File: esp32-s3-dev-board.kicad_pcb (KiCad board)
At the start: 2 copper layers, 30.8 x 50 mm, 16 parts, among them IC1 ESP32-S3-WROOM-1-N8R8, J1 Conn_01x18, J2 Conn_01x18, J3 PROG_HDR, Q1 SS8050-G, Q2 SS8050-G

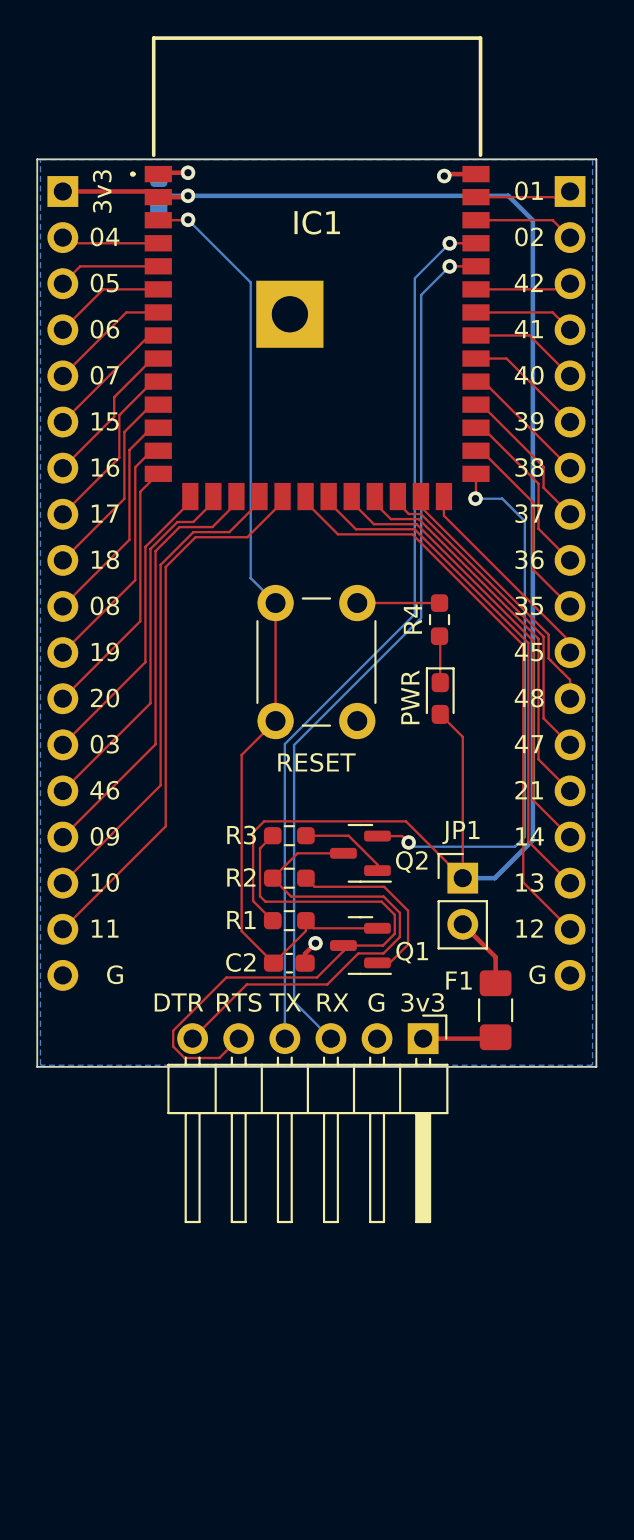
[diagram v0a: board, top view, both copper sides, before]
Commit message: Updated template for KiCAD 7
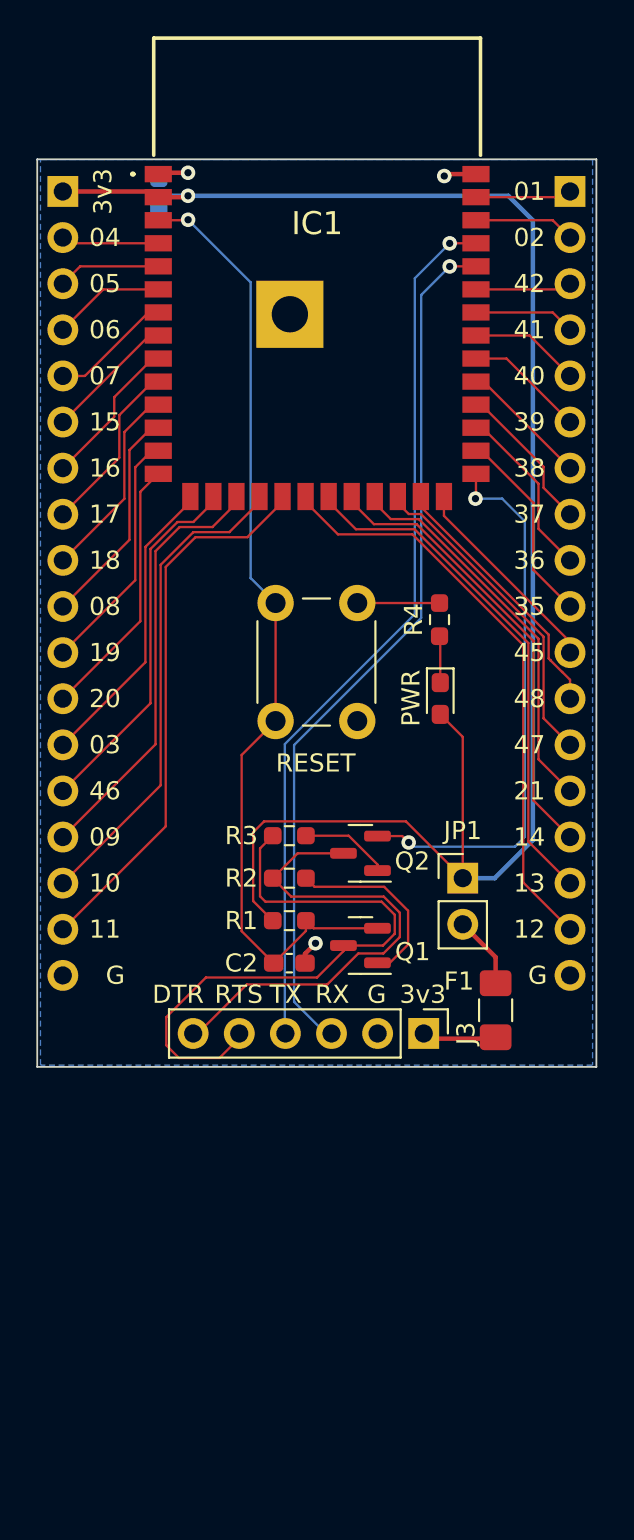
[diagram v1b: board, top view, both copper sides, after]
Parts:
- IC1: footprint footprints:ESP32S3WROOM1N8R8 -> Chof747 Footprints:ESP32S3WROOM1N8R8
- J3: footprint Connector_PinHeader_2.54mm:PinHeader_1x06_P2.54mm_Horizontal -> Connector_PinHeader_2.54mm:PinHeader_1x06_P2.54mm_Vertical
- moved J3 0.29 mm to (69.9, 119.8)
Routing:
- net RTS: track 32.3 -> 33.5 mm

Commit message: Changed reset circuit to UMH3N and Upgrade to KiCad 8
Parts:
- removed PWR: PWR, LED_SMD:LED_0603_1608Metric_Pad1.05x0.95mm_HandSolder
- removed Q2: SS8050-G, Package_TO_SOT_SMD:SOT-23
- removed R3: 10k, Resistor_SMD:R_0603_1608Metric_Pad0.98x0.95mm_HandSolder
- removed R4: 1k, Resistor_SMD:R_0603_1608Metric_Pad0.98x0.95mm_HandSolder
- removed RESET: SW_Reset, Button_Switch_THT:SW_PUSH_6mm
- added D1: PWR, LED_SMD:LED_0603_1608Metric_Pad1.05x0.95mm_HandSolder, F.Cu at (72.1, 106.1)
- added G***: LOGO, Chof747 Logos:LOGO large, B.Cu at (55.9, 87.6)
- added SW1: SW_Reset, Button_Switch_THT:SW_PUSH_6mm, F.Cu at (66.2, 96.0)
- Q1: value SS8050-G -> UMH3N; footprint Package_TO_SOT_SMD:SOT-23 -> Package_TO_SOT_SMD:SOT-363_SC-70-6
- R2: value 10k -> 1k
- moved R2 13.5 mm to (72.1, 101.8), turned to 90 degrees
- moved C2 2.21 mm to (61.6, 113.9), turned to 90 degrees
- moved R1 1.07 mm to (63.5, 113.9), turned to -90 degrees
- moved Q1 1.02 mm to (66.4, 113.9), turned to 90 degrees
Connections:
- Q1 pad 1: Net-(Q1-Pad1) -> RTS
- Q1 pad 2: ~{RESET} -> DTR
- Q1 pad 3: RTS ->  GPIO0
- R2 pad 1: DTR -> Net-(D1-K)
- R2 pad 2: Net-(Q1-Pad1) -> GND
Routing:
- net +3V3: track 95.3 -> 81.3 mm
- net DTR: track 27.3 -> 14.0 mm
- net RTS: track 33.5 -> 22.9 mm
- net Net-(Q1-Pad1): track 10.3 -> 0.00 mm
- net GND: track 9.33 -> 14.9 mm
- net Net-(Q2-Pad1): track 4.93 -> 0.00 mm
- net  GPIO0: track 30.6 -> 34.0 mm
- net Net-(D1-Pad1): track 2.57 -> 0.00 mm
- net Net-(D1-K): track 0.00 -> 2.51 mm
- net ~{RESET}: track 53.3 -> 51.6 mm
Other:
- board text added: "ESP32-S3 Dev. Board v1.1 (c)2024 chof"
- board text removed: "ESP32-S3 Dev. Board v1.0 (c)2022 chof"

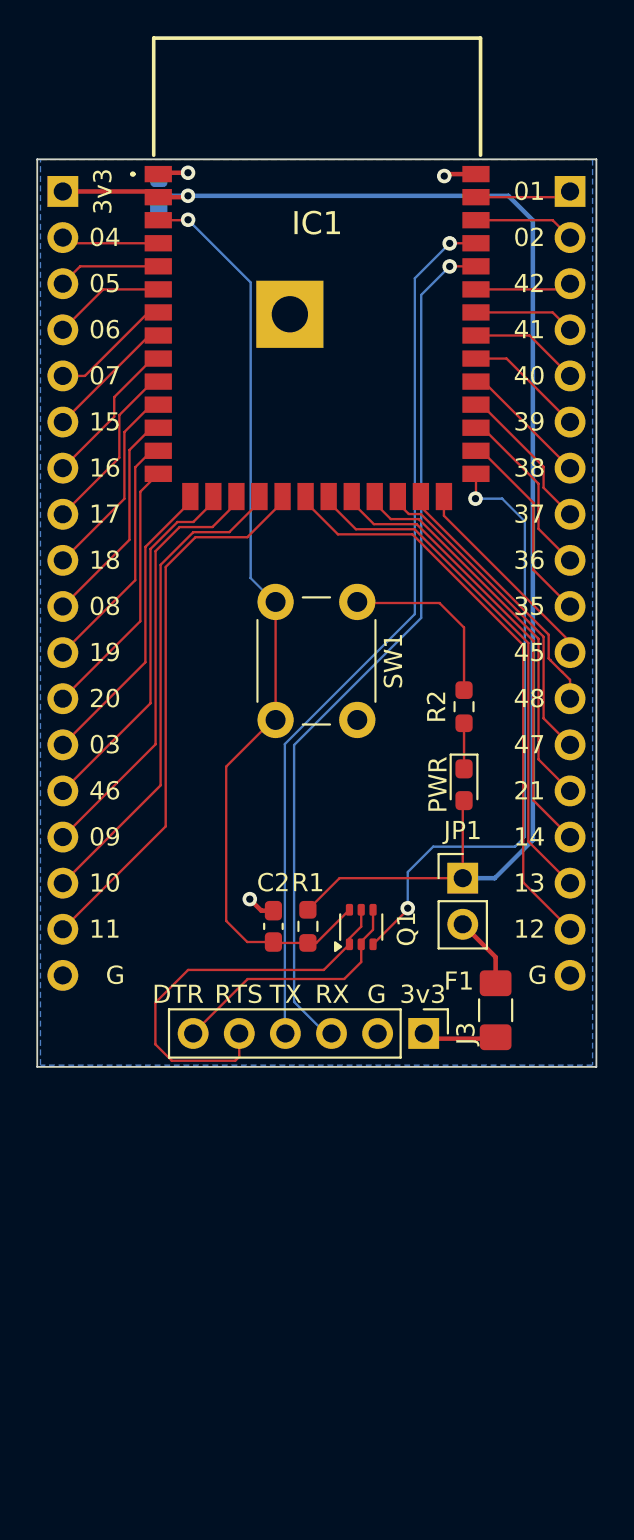
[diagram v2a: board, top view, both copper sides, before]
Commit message: Added version 1.1 with following changes:
- Changed reset and boot logic to UMH3 chip
- Added a boot button to allow manual setting into boot mode
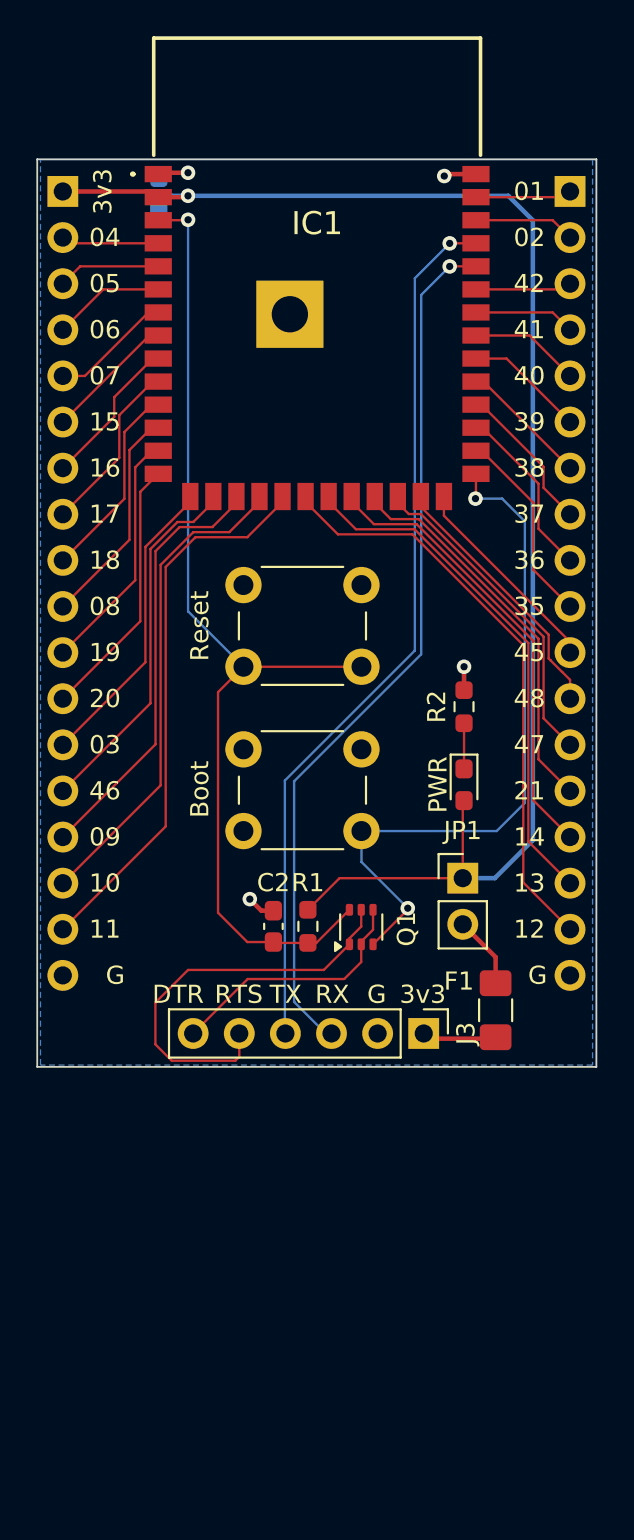
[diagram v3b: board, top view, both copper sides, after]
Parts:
- added SW2: Boot, Button_Switch_THT:SW_PUSH_6mm, F.Cu at (60.0, 104.2)
- SW1: value SW_Reset -> Reset
- moved SW1 6.34 mm to (60.0, 95.1), turned to 0 degrees
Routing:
- net GND: track 14.9 -> 6.31 mm, vias 3 -> 4
- net ~{RESET}: track 51.6 -> 56.8 mm
- net  GPIO0: track 34.0 -> 37.9 mm

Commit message: changed to slim board design - Made the board smaller so that it fits on a breadboard and leaves room for a slot on the left and right - Added a 3v3 Regulator to allow connection via an USB Breakout
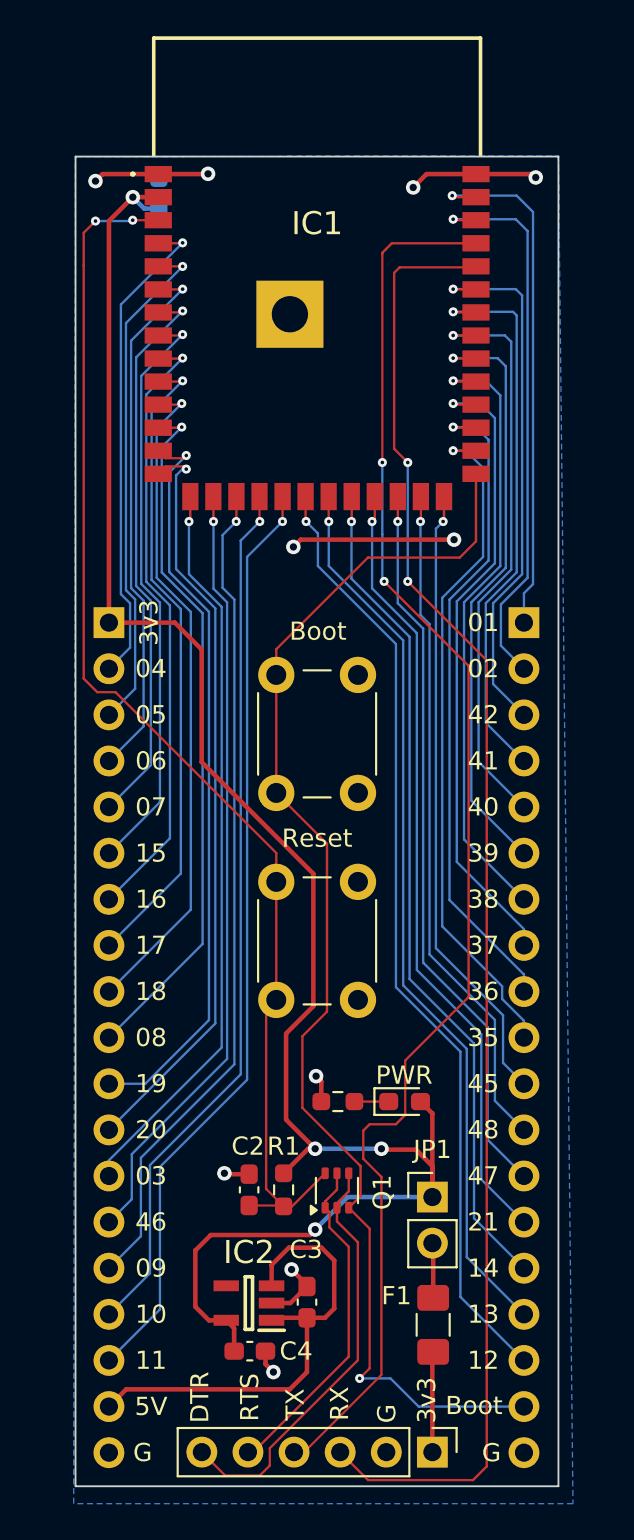
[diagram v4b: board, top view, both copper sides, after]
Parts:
- added C3: 1uF, Capacitor_SMD:C_0603_1608Metric_Pad1.08x0.95mm_HandSolder, F.Cu at (63.5, 134.6)
- added C4: 1uF, Capacitor_SMD:C_0603_1608Metric_Pad1.08x0.95mm_HandSolder, F.Cu at (60.3, 137.3)
- added IC2: ME6211C33M5G-N, Chof747 Footprints:SOT95P270X145-5N, F.Cu at (60.2, 134.7)
- J1, J2: footprint Connector_PinHeader_2.54mm:PinHeader_1x18_P2.54mm_Vertical -> Connector_PinHeader_2.54mm:PinHeader_1x19_P2.54mm_Vertical
- moved G*** 48.7 mm to (63.9, 135.7), turned to 90 degrees
- moved J1 23.9 mm to (52.5, 97.2)
- moved J2 23.9 mm to (75.4, 97.2)
- moved J3 23.1 mm to (70.4, 142.9)
- moved R2 22.8 mm to (65.2, 123.5), turned to 180 degrees
- moved D1 17.8 mm to (68.8, 123.5), turned to 0 degrees
- moved F1 17.7 mm to (70.4, 135.8)
- moved JP1 17.6 mm to (70.4, 128.8)
- moved SW1 17.5 mm to (66.3, 111.5), turned to -90 degrees
- moved C2 14.6 mm to (60.3, 128.4)
- moved Q1 14.6 mm to (65.1, 128.4)
- moved R1 14.6 mm to (62.2, 128.4)
- moved SW2 7.52 mm to (66.3, 100.0), turned to -90 degrees
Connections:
- net LP11_IO19 renamed ESP_USB_N
- net LP12_IO20 renamed ESP_USB_P
- J1 pad 18: GND -> +5V
- J2 pad 18: GND ->  GPIO0
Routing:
- net  GPIO0: track 37.9 -> 71.1 mm, vias 2 -> 1
- net ESP32_RX: track 48.4 -> 81.5 mm, vias 1 -> 2
- net ESP32_TX: track 49.0 -> 79.4 mm, vias 1 -> 2
- net ESP_USB_N: track 13.5 -> 41.1 mm, vias 0 -> 1
- net ESP_USB_P: track 14.6 -> 41.8 mm, vias 0 -> 1
- net RP10_IO37: track 8.36 -> 35.4 mm, vias 0 -> 1
- net RP11_IO38: track 7.16 -> 34.2 mm, vias 0 -> 1
- net RP09_IO36: track 9.66 -> 36.5 mm, vias 0 -> 1
- net RP08_IO35: track 10.9 -> 37.5 mm, vias 0 -> 1
- net RP12_IO39: track 6.63 -> 33.2 mm, vias 0 -> 1
- net +5V: track 0.00 -> 26.3 mm
- net LP10_IO8: track 12.2 -> 38.5 mm, vias 0 -> 1
- net LP09_IO18: track 11.0 -> 36.9 mm, vias 0 -> 1
- net RP13_IO40: track 6.10 -> 32.0 mm, vias 0 -> 1
- net LP08_IO17: track 9.66 -> 35.5 mm, vias 0 -> 1
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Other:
- board size 30.8 x 50 mm -> 26.6 x 73.2 mm
- board text added: "5V"
- board text added: "Boot"
